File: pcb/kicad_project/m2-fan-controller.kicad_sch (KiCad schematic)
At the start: 18 parts, among them J1 Bus_M.2_Socket_E, J2 Conn_01x04, J3 Conn_01x04, J4 JST PH_S2B-PH-K, J5 Conn_02x02_Odd_Even, U1 STM32F042F6P6

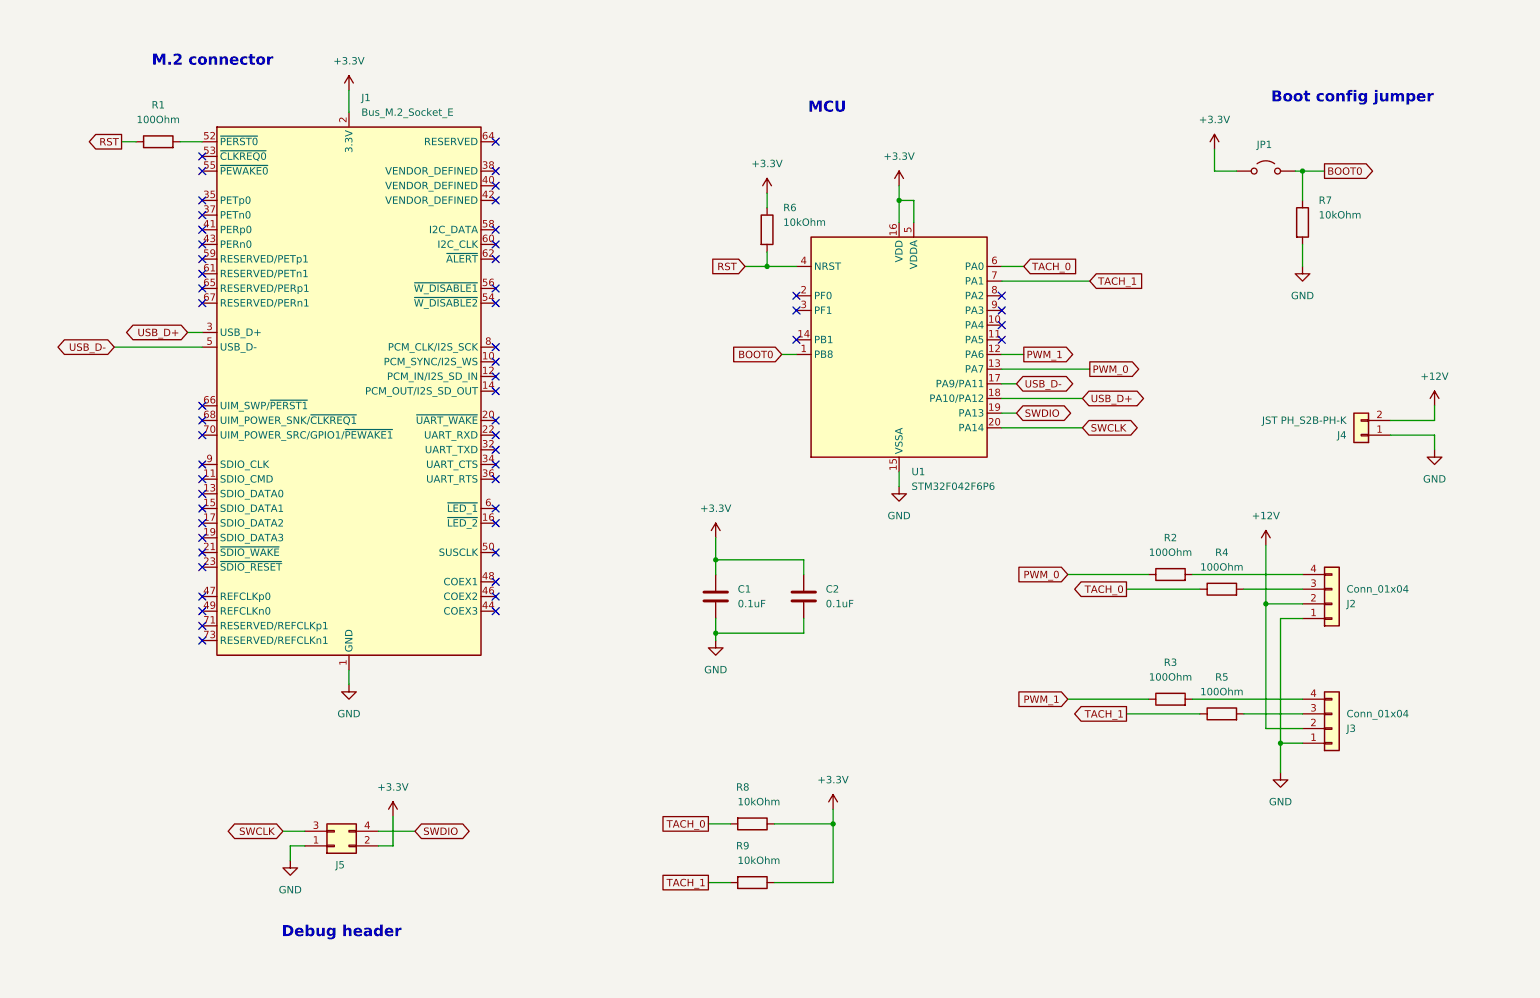
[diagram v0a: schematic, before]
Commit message: Implement power control for fans (#1)
* Final revision

* Use 0603 components
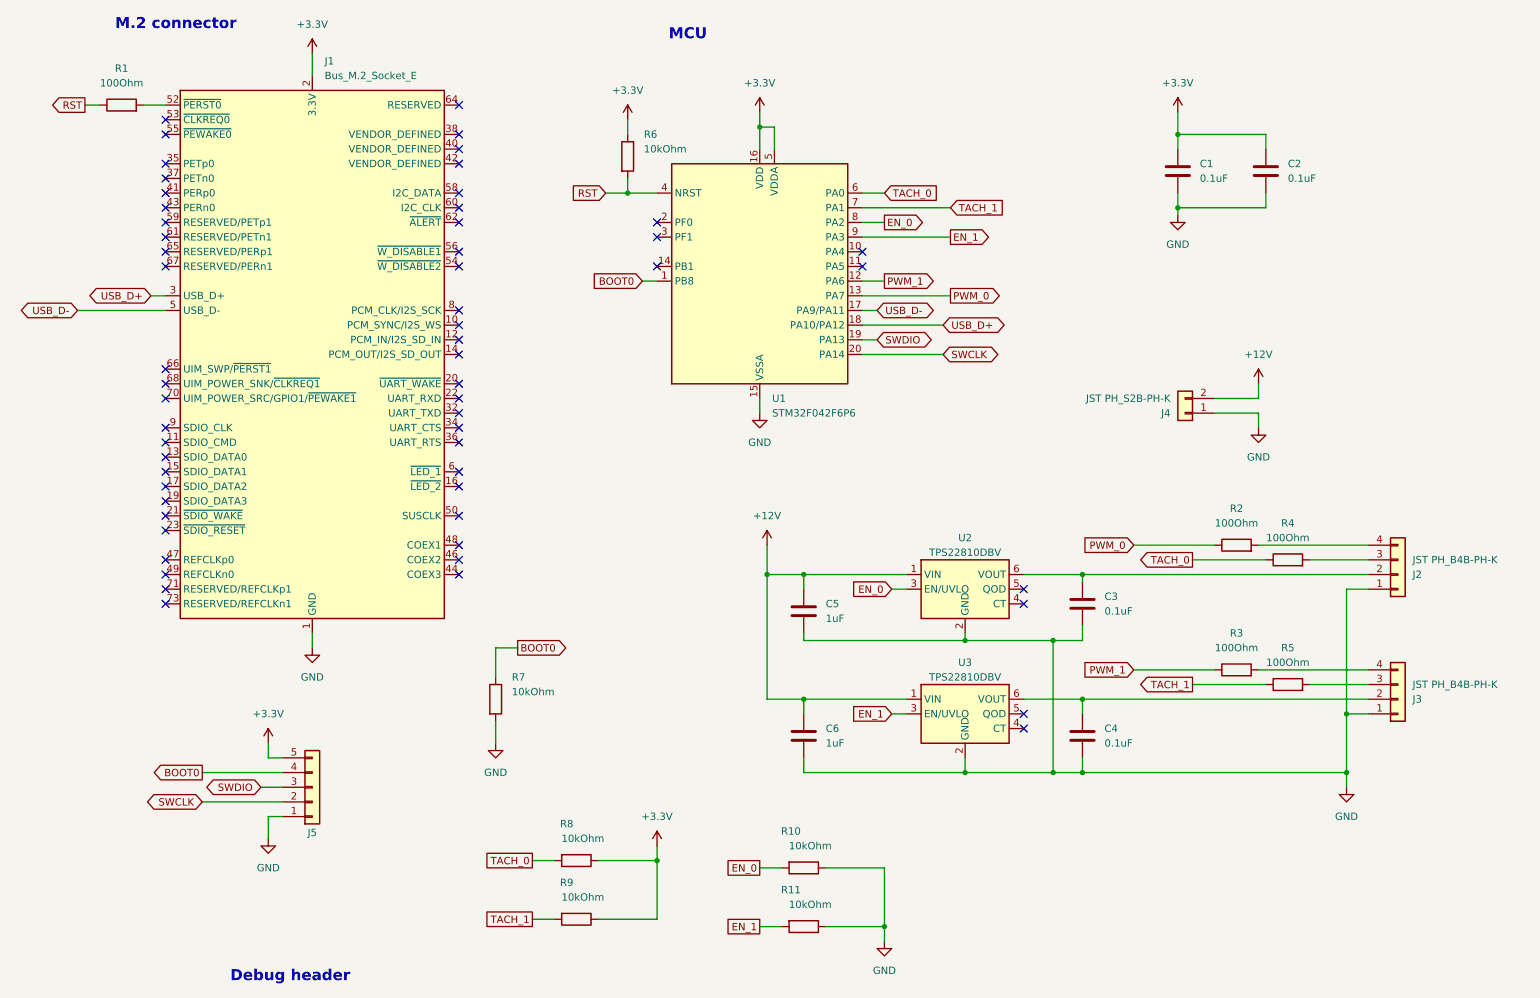
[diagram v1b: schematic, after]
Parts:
- removed JP1: Jumper_2_Open, Jumper:SolderJumper-2_P1.3mm_Open_RoundedPad1.0x1.5mm, symbol Jumper:Jumper_2_Open
- added C3, C4: 0.1uF, Capacitor_SMD:C_0603_1608Metric_Pad1.08x0.95mm_HandSolder, symbol Device:C
- added C5, C6: 1uF, Capacitor_SMD:C_0805_2012Metric_Pad1.18x1.45mm_HandSolder, symbol Device:C
- added R10, R11: 10kOhm, Resistor_SMD:R_0603_1608Metric_Pad0.98x0.95mm_HandSolder, symbol Device:R
- added U2, U3: TPS22810DBV, Package_TO_SOT_SMD:SOT-23-6, symbol Power_Management:TPS22810DBV
- C1, C2: footprint Capacitor_SMD:C_0805_2012Metric_Pad1.18x1.45mm_HandSolder -> Capacitor_SMD:C_0603_1608Metric_Pad1.08x0.95mm_HandSolder
- J2, J3: value Conn_01x04 -> JST PH_B4B-PH-K; footprint Connector:FanPinHeader_1x04_P2.54mm_Vertical -> Connector_JST:JST_PH_B4B-PH-K_1x04_P2.00mm_Vertical
- J4: footprint Connector_JST:JST_PH_S2B-PH-K_1x02_P2.00mm_Horizontal -> Connector_JST:JST_PH_B2B-PH-K_1x02_P2.00mm_Vertical
- J5: footprint Connector_PinHeader_2.54mm:PinHeader_1x04_P2.54mm_Vertical -> Connector_PinHeader_1.27mm:PinHeader_1x05_P1.27mm_Vertical; symbol Connector_Generic:Conn_02x02_Odd_Even -> Connector_Generic:Conn_01x05
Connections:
- net +12V: now also C5.1, C6.1, U2.1 (VIN), U3.1 (VIN); no longer J2.2 (Pin_2), J3.2 (Pin_2)
- net +3.3V: now also J5.5 (Pin_5); no longer J5.2 (Pin_2)
- net BOOT0: now also J5.4 (Pin_4)
- net GND: now also C3.2, C4.2, C5.2, C6.2, R10.1, R11.1, U2.2 (GND), U3.2 (GND)
- net SWCLK: now also J5.2 (Pin_2); no longer J5.3 (Pin_3)
- net SWDIO: now also J5.3 (Pin_3); no longer J5.4 (Pin_4)
- net EN_0: now reaches U1.8 (PA2)
- net EN_0: now also R10.2, U2.3 (EN/UVLO)
- net EN_1: now reaches U1.9 (PA3)
- net EN_1: now also R11.2, U3.3 (EN/UVLO)
- new net: C3.1, J2.2 (Pin_2), U2.6 (VOUT)
- new net: C4.1, J3.2 (Pin_2), U3.6 (VOUT)
- no-connect marks 56 -> 58
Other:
- note removed: "Boot config jumper"
- moved on the sheet: C1, C2, J1, J2, J3, J4, R1, R2, R3, R4, R5, R6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
